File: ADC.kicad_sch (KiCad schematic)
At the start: 18 parts

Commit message: Final Schematic
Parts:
- UE1, UE2, UE3, UE4, UE5, UE6: footprint (none) -> MCP3424-E_SL:SOIC127P600X175-14N
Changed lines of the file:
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@@
       (effects (font (size 1.27 1.27)) (justify left))
     )
-    (property "Footprint" "" (id 2) (at 242.57 59.69 0)
+    (property "Footprint" "MCP3424-E_SL:SOIC127P600X175-14N" (id 2) (at 242.57 59.69 0)
       (effects (font (size 1.27 1.27)) hide)
     )
@@
       (effects (font (size 1.27 1.27)) (justify left))
     )
-    (property "Footprint" "" (id 2) (at 160.02 69.85 0)
+    (property "Footprint" "MCP3424-E_SL:SOIC127P600X175-14N" (id 2) (at 160.02 69.85 0)
       (effects (font (size 1.27 1.27)) hide)
     )
@@
       (effects (font (size 1.27 1.27)) (justify left))
     )
-    (property "Footprint" "" (id 2) (at 73.66 153.67 0)
+    (property "Footprint" "MCP3424-E_SL:SOIC127P600X175-14N" (id 2) (at 73.66 153.67 0)
       (effects (font (size 1.27 1.27)) hide)
     )
@@
       (effects (font (size 1.27 1.27)) (justify left))
     )
-    (property "Footprint" "" (id 2) (at 165.1 167.64 0)
+    (property "Footprint" "MCP3424-E_SL:SOIC127P600X175-14N" (id 2) (at 165.1 167.64 0)
       (effects (font (size 1.27 1.27)) hide)
     )
@@
       (effects (font (size 1.27 1.27)) (justify left))
     )
-    (property "Footprint" "" (id 2) (at 73.66 60.96 0)
+    (property "Footprint" "MCP3424-E_SL:SOIC127P600X175-14N" (id 2) (at 73.66 60.96 0)
       (effects (font (size 1.27 1.27)) hide)
     )
@@
       (effects (font (size 1.27 1.27)) (justify left))
     )
-    (property "Footprint" "" (id 2) (at 241.3 133.35 0)
-      (effects (font (size 1.27 1.27)) hide)
-    )
+    (property "Footprint" "MCP3424-E_SL:SOIC127P600X175-14N" (id 2) (at 241.3 133.35 0)
+      (effects (font (size 1.27 1.27)) hide)
+    )

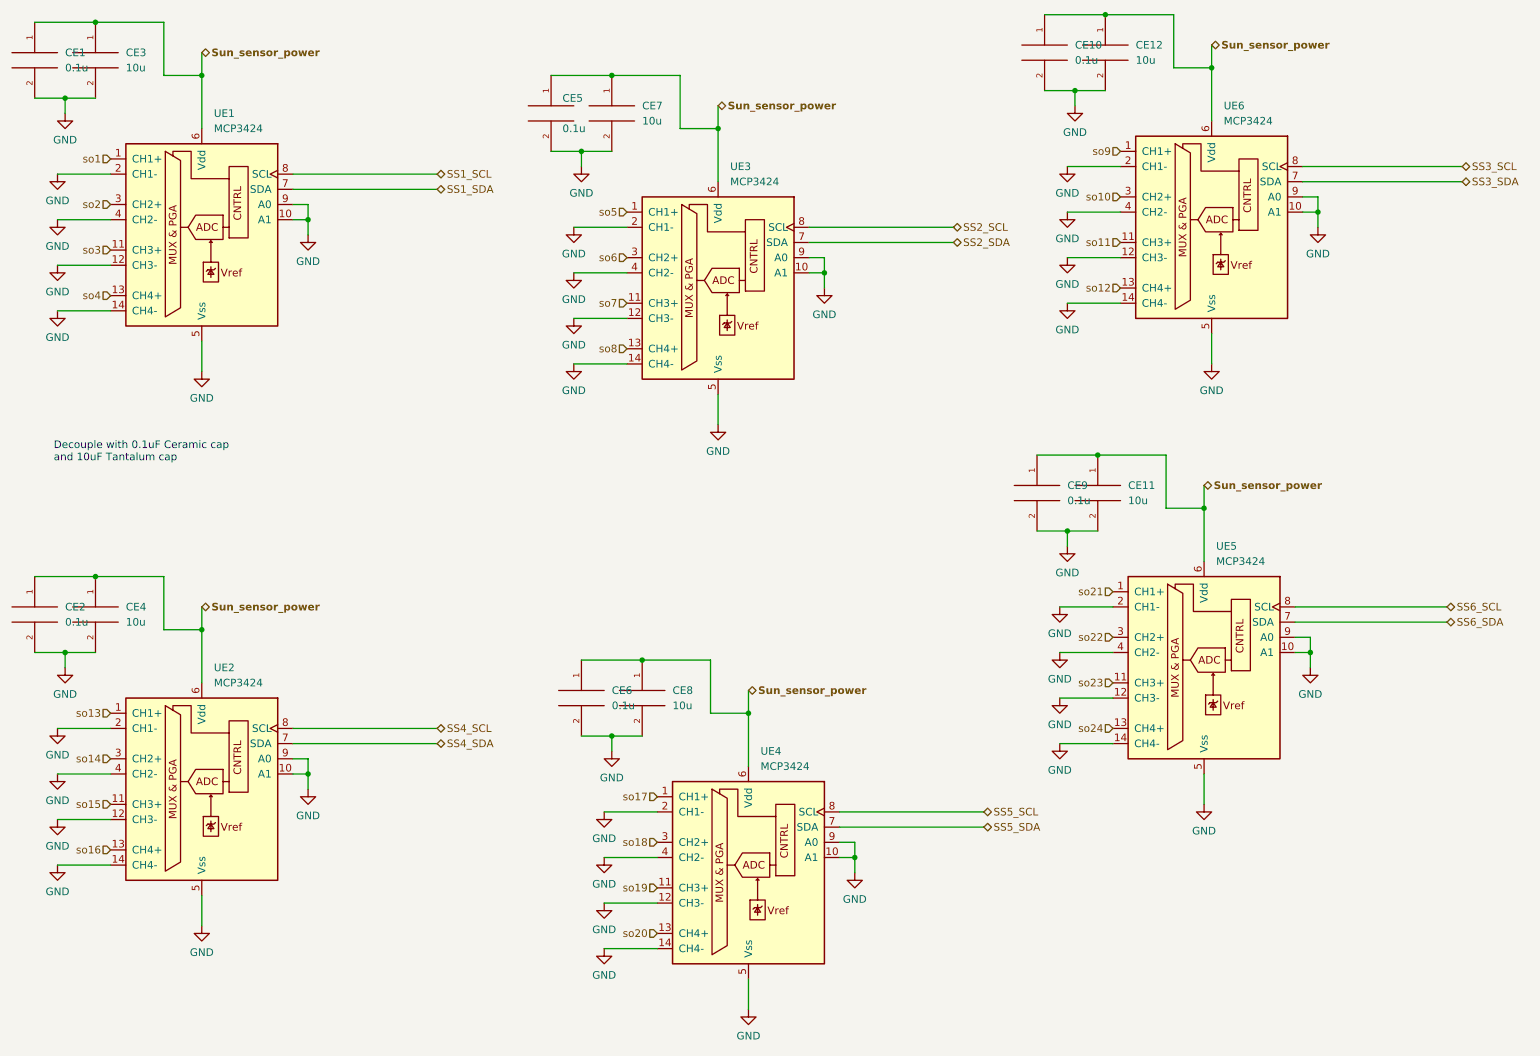
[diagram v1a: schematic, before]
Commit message: MCU circuitry forgot LOL
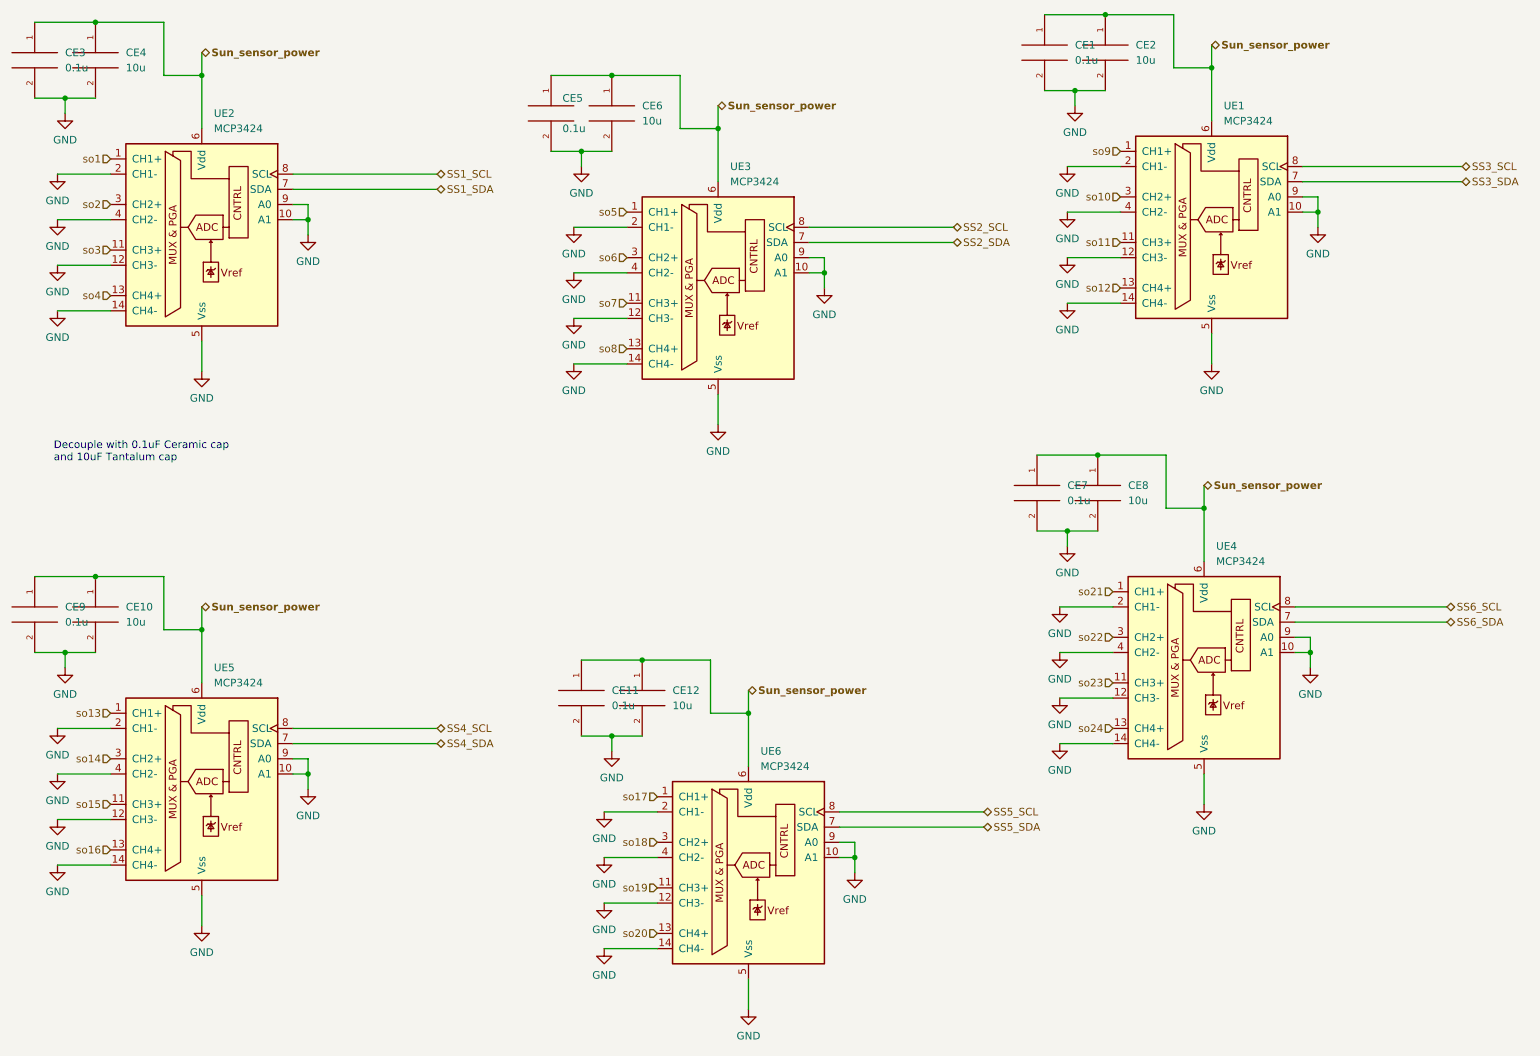
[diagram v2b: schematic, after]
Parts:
- renumbered CE10 to CE1, CE4 to CE10, CE6 to CE11, CE8 to CE12, CE12 to CE2, CE1 to CE3, CE3 to CE4, CE7 to CE6, CE9 to CE7, CE11 to CE8, CE2 to CE9, UE6 to UE1, UE1 to UE2, UE5 to UE4, UE2 to UE5, UE4 to UE6

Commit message: ADC tantalum cap PN added
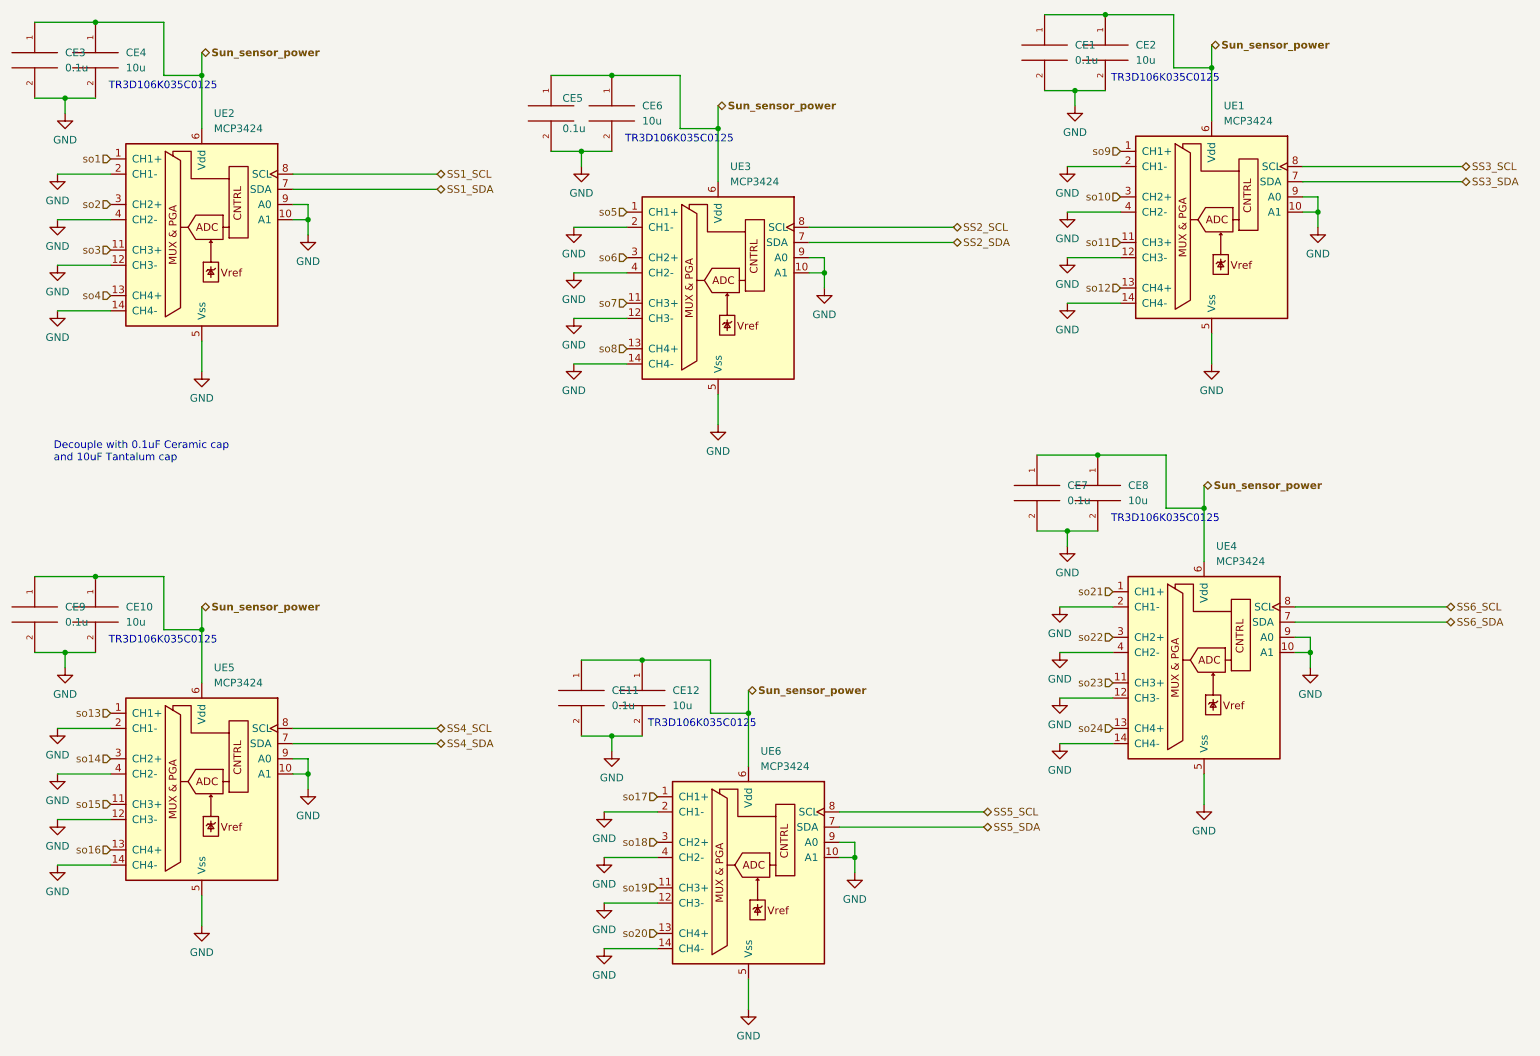
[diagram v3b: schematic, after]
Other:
- note added: "TR3D106K035C0125"
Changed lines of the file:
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@@
+    (effects (font (size 1.27 1.27)) (justify left bottom))
+  )
+  (text "\n    TR3D106K035C0125" (at 123.19 143.51 0)
+    (effects (font (size 1.27 1.27)) (justify left bottom))
+  )
+  (text "\n    TR3D106K035C0125" (at 200.66 109.22 0)
+    (effects (font (size 1.27 1.27)) (justify left bottom))
+  )
+  (text "\n    TR3D106K035C0125" (at 119.38 45.72 0)
+    (effects (font (size 1.27 1.27)) (justify left bottom))
+  )
+  (text "\n    TR3D106K035C0125" (at 33.02 36.83 0)
+    (effects (font (size 1.27 1.27)) (justify left bottom))
+  )
+  (text "\n    TR3D106K035C0125" (at 33.02 129.54 0)
+    (effects (font (size 1.27 1.27)) (justify left bottom))
+  )
+  (text "\n    TR3D106K035C0125" (at 200.66 35.56 0)
     (effects (font (size 1.27 1.27)) (justify left bottom))
   )
